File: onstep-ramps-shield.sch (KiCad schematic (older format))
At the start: 0 parts

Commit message: Schematic, initial board layout
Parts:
- added BME280, DS3231: Conn_01x08, Connector_PinSocket_2.54mm:PinSocket_1x08_P2.54mm_Vertical, symbol Connector_Generic:Conn_01x08
- added BZ1: Buzzer, Buzzer_Beeper:Buzzer_12x9.5RM7.6, symbol Device:Buzzer
- added DEC1, FOC1, FOC2, RA1: RJ12, Connector_RJ:RJ12_Amphenol_54601, symbol Connector:RJ12
- added J_AUX1: RAMPS_AUX1, Connector_PinSocket_2.54mm:PinSocket_2x04_P2.54mm_Vertical, symbol OnstepRampsShield:RAMPS_AUX1
- added J_AUX2: RAMPS_AUX2, Connector_PinSocket_2.54mm:PinSocket_2x05_P2.54mm_Vertical, symbol OnstepRampsShield:RAMPS_AUX2
- added J_AUX3: RAMPS_AUX3, Connector_PinSocket_2.54mm:PinSocket_2x04_P2.54mm_Vertical, symbol OnstepRampsShield:RAMPS_AUX3
- added J_AUX4: RAMPS_AUX-4, Connector_PinSocket_2.54mm:PinSocket_1x18_P2.54mm_Vertical, symbol OnstepRampsShield:RAMPS_AUX-4
- added J_DEC1, J_FOC1, J_FOC2, J_RA1: RAMPS_MOTOR, Connector_PinSocket_2.54mm:PinSocket_1x04_P2.54mm_Vertical, symbol OnstepRampsShield:RAMPS_MOTOR
- added J_I2C1: RAMPS_I2C, Connector_PinSocket_2.54mm:PinSocket_1x04_P2.54mm_Vertical, symbol OnstepRampsShield:RAMPS_I2C
- added J_PEC1, J_RET1: AudioJack3, Connector_Audio:Jack_3.5mm_CUI_SJ1-3533NG_Horizontal, symbol Connector:AudioJack3
- added J_SER1: RAMPS_ENDSTOPS, Connector_PinSocket_2.54mm:PinSocket_1x02_P2.54mm_Vertical, symbol OnstepRampsShield:RAMPS_ENDSTOPS
- added J_SERV1: RAMPS_SERVOS_SER1, Connector_PinSocket_2.54mm:PinSocket_1x03_P2.54mm_Vertical, symbol OnstepRampsShield:RAMPS_SERVOS_SER1
- added J_SERV2: RAMPS_SERVOS_SER2, Connector_PinSocket_2.54mm:PinSocket_1x03_P2.54mm_Vertical, symbol OnstepRampsShield:RAMPS_SERVOS_SER2
- added J_SERV3: RAMPS_SERVOS_SER3, Connector_PinSocket_2.54mm:PinSocket_1x03_P2.54mm_Vertical, symbol OnstepRampsShield:RAMPS_SERVOS_SER3
- added J_SERV4: RAMPS_SERVOS_SER4, Connector_PinSocket_2.54mm:PinSocket_1x03_P2.54mm_Vertical, symbol OnstepRampsShield:RAMPS_SERVOS_SER4
- added R1: 2k, Resistor_THT:R_Axial_DIN0204_L3.6mm_D1.6mm_P5.08mm_Horizontal, symbol Device:R
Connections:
- new net: BZ1.2 (+), J_SERV4.1 (GND)
- new net: BZ1.1 (-), J_SERV4.3 (D4)
- new net: J_RET1.S, R1.2
- new net CS_BME280: BME280.7 (Pin_7), J_AUX3.2 (D49)
- new net CS_DS3234: J_AUX3.6 (D53)
- new net E0_1A: FOC1.3, J_FOC1.3 (1A)
- new net E0_1B: FOC1.4, J_FOC1.4 (1B)
- new net E0_2A: FOC1.2, J_FOC1.2 (2A)
- new net E0_2B: FOC1.1, J_FOC1.1 (2B)
- new net E1_1A: FOC2.3, J_FOC2.3 (1A)
- new net E1_1B: FOC2.4, J_FOC2.4 (1B)
- new net E1_2A: FOC2.2, J_FOC2.2 (2A)
- new net E1_2B: FOC2.1, J_FOC2.1 (2B)
- new net GND: BME280.1 (Pin_1), DS3231.1 (Pin_1), J_AUX1.3 (GND), J_AUX1.4 (GND), J_AUX2.2 (GND), J_AUX3.7 (GND), J_AUX4.2 (GND), J_I2C1.2 (GND), J_PEC1.S, J_SERV1.1 (GND), J_SERV2.1 (GND), J_SERV3.1 (GND)
- new net PEC: J_AUX1.5 (A3), J_PEC1.R
- new net RETICULE_LED: J_SERV3.3 (D5), R1.1
- new net RX1: J_SER1.2 (D19)
- new net RX2: J_AUX4.17 (D17)
- new net SCK: BME280.4 (Pin_4), J_AUX3.5 (SCK)
- new net SCL: DS3231.4 (Pin_4), J_I2C1.4 (SCL)
- new net SDA: DS3231.3 (Pin_3), J_I2C1.3 (SDA)
- new net SDI: BME280.6 (Pin_6), J_AUX3.3 (MISO)
- new net SDO: BME280.5 (Pin_5), J_AUX3.4 (MOSI)
- new net STATUS_LED: J_SERV1.3 (D11)
- new net STATUS_LED2: J_SERV2.3 (D6)
- new net TX1: J_SER1.1 (D18)
- new net TX2: J_AUX4.18 (D16)
- new net VCC: BME280.3 (Pin_3), DS3231.2 (Pin_2), J_AUX1.1 (VCC), J_AUX1.2 (VCC), J_AUX2.1 (VCC), J_AUX3.1 (VCC), J_AUX4.1 (VCC), J_I2C1.1 (VCC), J_PEC1.T, J_RET1.T, J_SERV1.2 (VCC), J_SERV2.2 (VCC), J_SERV3.2 (VCC), J_SERV4.2 (VCC)
- new net X_1A: J_RA1.3 (1A), RA1.3
- new net X_1B: J_RA1.4 (1B), RA1.4
- new net X_2A: J_RA1.2 (2A), RA1.2
- new net X_2B: J_RA1.1 (2B), RA1.1
- new net X_AUX1: J_AUX4.13 (D29)
- new net X_M0: J_AUX4.16 (D23)
- new net X_M1: J_AUX4.15 (D25)
- new net X_M2: J_AUX4.14 (D27)
- new net Y_1A: DEC1.3, J_DEC1.3 (1A)
- new net Y_1B: DEC1.4, J_DEC1.4 (1B)
- new net Y_2A: DEC1.2, J_DEC1.2 (2A)
- new net Y_2B: DEC1.1, J_DEC1.1 (2B)
- new net Y_AUX1: J_AUX4.9 (D37)
- new net Y_M0: J_AUX4.12 (D31)
- new net Y_M1: J_AUX4.11 (D33)
- new net Y_M2: J_AUX4.10 (D35)
- no-connect marks 0 -> 33

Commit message: Routing
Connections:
- net GND: now also BZ1.2 (+); no longer BME280.1 (Pin_1), DS3231.1 (Pin_1), J_AUX1.3 (GND), J_AUX1.4 (GND), J_AUX2.2 (GND), J_AUX3.7 (GND), J_I2C1.2 (GND), J_SERV1.1 (GND), J_SERV2.1 (GND), J_SERV3.1 (GND)
- net VCC: no longer BME280.3 (Pin_3), DS3231.2 (Pin_2), J_AUX1.1 (VCC), J_AUX1.2 (VCC), J_AUX2.1 (VCC), J_AUX3.1 (VCC), J_I2C1.1 (VCC), J_SERV1.2 (VCC), J_SERV2.2 (VCC), J_SERV3.2 (VCC), J_SERV4.2 (VCC)
- net at J_SERV4.1 (GND): no longer BZ1.2 (+)
- net BUZZER: now reaches BZ1.1 (-), J_SERV4.3 (D4)
- new net I2C_GND: DS3231.1 (Pin_1), J_I2C1.2 (GND)
- new net I2C_VCC: DS3231.2 (Pin_2), J_I2C1.1 (VCC)
- new net SPI_GND: BME280.1 (Pin_1), J_AUX3.7 (GND)
- new net SPI_VCC: BME280.3 (Pin_3), J_AUX3.1 (VCC)
- no-connect marks 33 -> 47
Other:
- moved on the sheet: BZ1
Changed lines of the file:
@@
 	0    -1   -1   0
 $EndComp
-Text GLabel 2350 6700 0    50   Input ~ 0
-VCC
-Text GLabel 3750 6750 0    50   Input ~ 0
-VCC
 Text GLabel 5100 4650 0    50   Input ~ 0
 VCC
 Text GLabel 5550 2250 2    50   Input ~ 0
-VCC
-Text GLabel 2950 6700 2    50   Input ~ 0
-GND
-Text GLabel 3750 7050 0    50   Input ~ 0
-GND
+I2C_VCC
 Text GLabel 5100 4550 0    50   Input ~ 0
 GND
 Text GLabel 5550 2350 2    50   Input ~ 0
-GND
+I2C_GND
 Text GLabel 1000 1800 3    50   Input ~ 0
 E0_2B
@@
 L Device:Buzzer BZ1
 U 1 1 5F550329
-P 2600 5300
-F 0 "BZ1" V 2651 5113 50  0000 R CNN
-F 1 "Buzzer" V 2560 5113 50  0000 R CNN
-F 2 "Buzzer_Beeper:Buzzer_12x9.5RM7.6" V 2575 5400 50  0001 C CNN
-F 3 "~" V 2575 5400 50  0001 C CNN
-	1    2600 5300
-	0    -1   -1   0
-$EndComp
-Wire Wire Line
-	2500 5850 2500 5400
-Wire Wire Line
-	2700 5400 2700 5850
+P 7300 4100
+F 0 "BZ1" V 7351 3913 50  0000 R CNN
+F 1 "Buzzer" V 7260 3913 50  0000 R CNN
+F 2 "Buzzer_Beeper:Buzzer_12x9.5RM7.6" V 7275 4200 50  0001 C CNN
+F 3 "~" V 7275 4200 50  0001 C CNN
+	1    7300 4100
+	0    -1   -1   0
+$EndComp
 Text GLabel 4350 6950 2    50   Input ~ 0
 CS_DS3234
@@
 Text GLabel 7450 1250 2    50   Input ~ 0
 CS_BME280
-Text GLabel 7450 1850 2    50   Input ~ 0
-GND
-Text GLabel 7450 1650 2    50   Input ~ 0
-VCC
-Text GLabel 7450 3200 2    50   Input ~ 0
-VCC
 Text GLabel 7450 3300 2    50   Input ~ 0
-GND
+I2C_GND
 Text GLabel 4350 6750 2    50   Input ~ 0
 CS_BME280
@@
 	0    -1   -1   0
 $EndComp
-Text GLabel 1450 6800 2    50   Input ~ 0
-GND
-Text GLabel 1450 6700 2    50   Input ~ 0
-VCC
-Text GLabel 850  6800 0    50   Input ~ 0
-GND
-Text GLabel 850  6700 0    50   Input ~ 0
-VCC
-Text GLabel 2700 4500 1    50   Input ~ 0
-GND
-Text GLabel 2600 4500 1    50   Input ~ 0
-VCC
-Text GLabel 2600 5850 1    50   Input ~ 0
-VCC
-Text GLabel 1250 5850 1    50   Input ~ 0
-GND
-Text GLabel 1150 5850 1    50   Input ~ 0
-VCC
-Text GLabel 1200 4500 1    50   Input ~ 0
-GND
-Text GLabel 1100 4500 1    50   Input ~ 0
-VCC
 $Comp
 L Connector_Generic:Conn_01x08 BME280
@@
 NoConn ~ 7450 2700
 NoConn ~ 7450 2600
+Text GLabel 7450 3200 2    50   Input ~ 0
+I2C_VCC
+Text GLabel 3750 6750 0    50   Input ~ 0
+SPI_VCC
+Text GLabel 3750 7050 0    50   Input ~ 0
+SPI_GND
+Text GLabel 7450 1650 2    50   Input ~ 0
+SPI_VCC
+Text GLabel 7450 1850 2    50   Input ~ 0
+SPI_GND
+NoConn ~ 2600 4500
+NoConn ~ 2700 4500
+NoConn ~ 1100 4500
+NoConn ~ 1200 4500
+NoConn ~ 1150 5850
+NoConn ~ 1250 5850
+NoConn ~ 2600 5850
+NoConn ~ 2700 5850
+Text GLabel 2500 5850 1    50   Input ~ 0
+BUZZER
+Text GLabel 7200 4200 3    50   Input ~ 0
+BUZZER
+Text GLabel 7400 4200 3    50   Input ~ 0
+GND
+NoConn ~ 2350 6700
+NoConn ~ 2950 6700
+NoConn ~ 850  6700
+NoConn ~ 850  6800
+NoConn ~ 1450 6800
+NoConn ~ 1450 6700
 $EndSCHEMATC

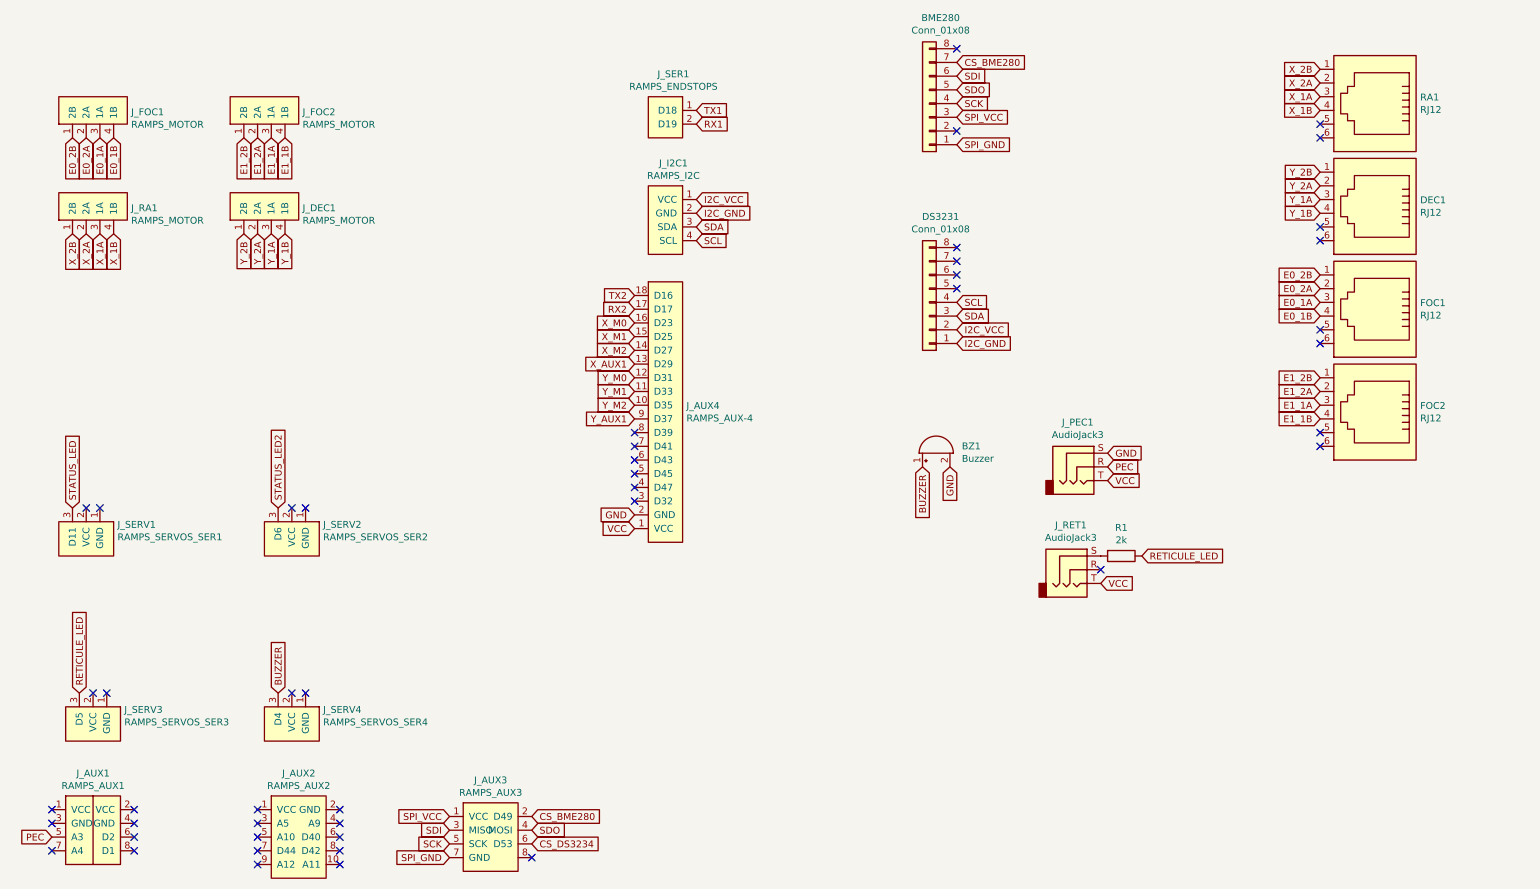
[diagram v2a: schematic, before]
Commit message: Include HC05
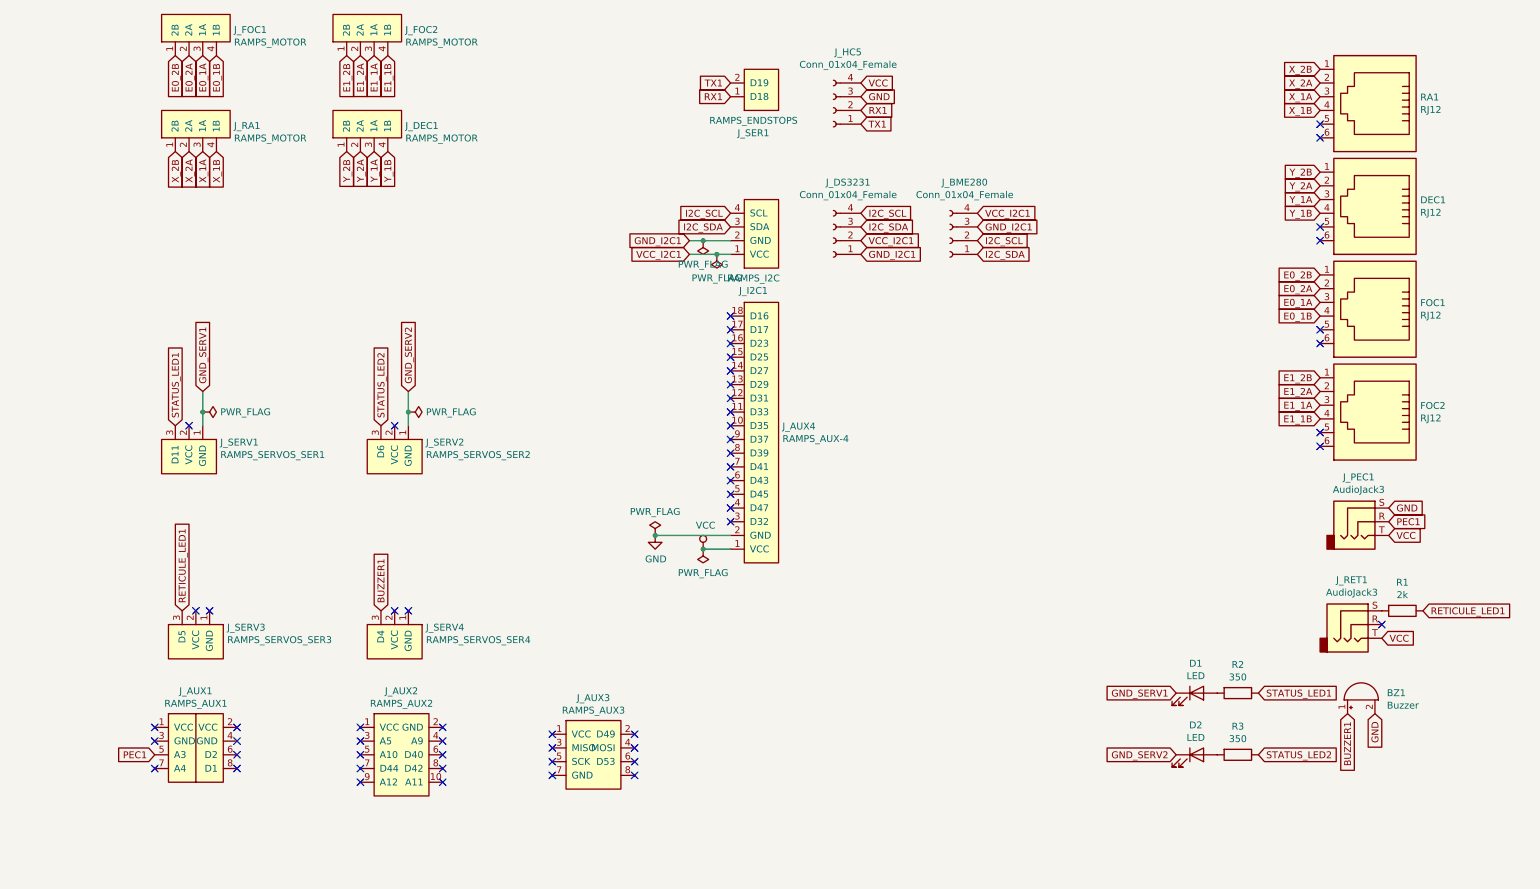
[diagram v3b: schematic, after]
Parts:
- removed BME280, DS3231: Conn_01x08, Connector_PinSocket_2.54mm:PinSocket_1x08_P2.54mm_Vertical, symbol Connector_Generic:Conn_01x08
- added D1, D2: LED, LED_SMD:LED_0603_1608Metric_Pad1.05x0.95mm_HandSolder, symbol Device:LED
- added J_BME280, J_DS3231, J_HC5: Conn_01x04_Female, Connector_PinSocket_2.54mm:PinSocket_1x04_P2.54mm_Vertical, symbol Connector:Conn_01x04_Female
- added R2, R3: 350, Resistor_SMD:R_0603_1608Metric_Pad1.05x0.95mm_HandSolder, symbol Device:R
- R1: footprint Resistor_THT:R_Axial_DIN0204_L3.6mm_D1.6mm_P5.08mm_Horizontal -> Resistor_SMD:R_0603_1608Metric_Pad1.05x0.95mm_HandSolder
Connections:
- net GND: now also J_HC5.3 (Pin_3)
- net RX1: now also J_SER1.1 (D18), J_HC5.2 (Pin_2); no longer J_SER1.2 (D19)
- net STATUS_LED2: now also R3.1
- net TX1: now also J_SER1.2 (D19), J_HC5.1 (Pin_1); no longer J_SER1.1 (D18)
- net VCC: now also J_HC5.4 (Pin_4)
- net GND_SERV1: now reaches J_SERV1.1 (GND)
- net GND_SERV1: now also D1.1 (K)
- net GND_SERV2: now reaches J_SERV2.1 (GND)
- net GND_SERV2: now also D2.1 (K)
- net BUZZER renamed BUZZER1
- net CS_BME280: no longer names the net of J_AUX3.2 (D49)
- net CS_DS3234: no longer names the net of J_AUX3.6 (D53)
- net I2C_GND renamed GND_I2C1
- net GND_I2C1: now also J_BME280.3 (Pin_3), J_DS3231.1 (Pin_1)
- net I2C_VCC renamed VCC_I2C1
- net VCC_I2C1: now also J_BME280.4 (Pin_4), J_DS3231.2 (Pin_2)
- net PEC renamed PEC1
- net RETICULE_LED renamed RETICULE_LED1
- net RX2: no longer names the net of J_AUX4.17 (D17)
- net SCK: no longer names the net of J_AUX3.5 (SCK)
- net SCL renamed I2C_SCL
- net I2C_SCL: now also J_BME280.2 (Pin_2), J_DS3231.4 (Pin_4)
- net SDA renamed I2C_SDA
- net I2C_SDA: now also J_BME280.1 (Pin_1), J_DS3231.3 (Pin_3)
- net SDI: no longer names the net of J_AUX3.3 (MISO)
- net SDO: no longer names the net of J_AUX3.4 (MOSI)
- net SPI_GND: no longer names the net of J_AUX3.7 (GND)
- net SPI_VCC: no longer names the net of J_AUX3.1 (VCC)
- net STATUS_LED renamed STATUS_LED1
- net STATUS_LED1: now also R2.1
- net TX2: no longer names the net of J_AUX4.18 (D16)
- net X_AUX1: no longer names the net of J_AUX4.13 (D29)
- net X_M0: no longer names the net of J_AUX4.16 (D23)
- net X_M1: no longer names the net of J_AUX4.15 (D25)
- net X_M2: no longer names the net of J_AUX4.14 (D27)
- net Y_AUX1: no longer names the net of J_AUX4.9 (D37)
- net Y_M0: no longer names the net of J_AUX4.12 (D31)
- net Y_M1: no longer names the net of J_AUX4.11 (D33)
- net Y_M2: no longer names the net of J_AUX4.10 (D35)
- new net: D1.2 (A), R2.2
- new net: D2.2 (A), R3.2
- no-connect marks 47 -> 56
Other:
- moved on the sheet: BZ1, J_AUX1, J_AUX2, J_AUX3, J_AUX4, J_DEC1, J_FOC1, J_FOC2, J_I2C1, J_PEC1, J_RA1, J_RET1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

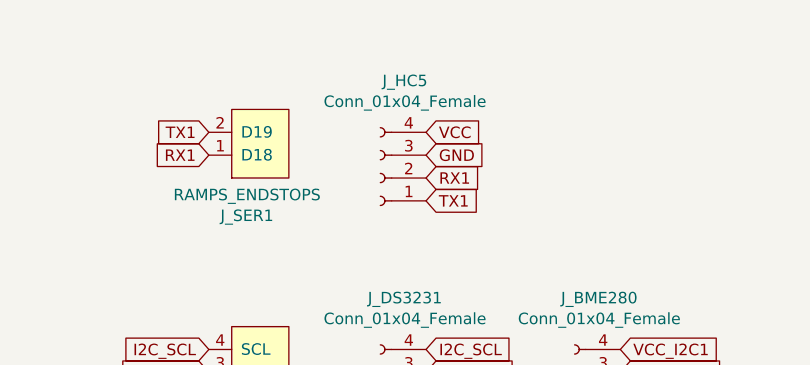
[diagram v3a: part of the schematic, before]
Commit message: Reorder components
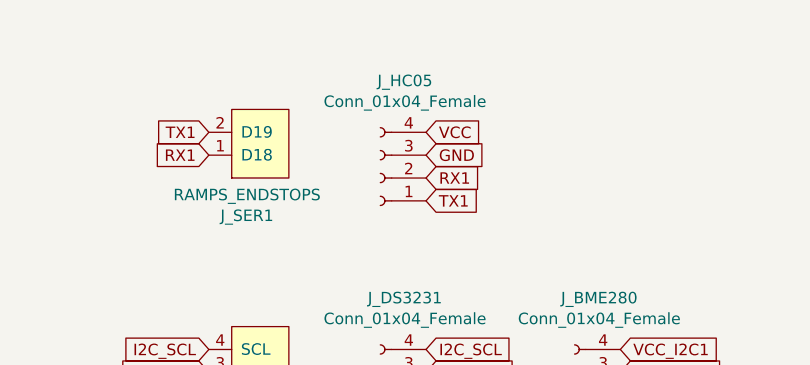
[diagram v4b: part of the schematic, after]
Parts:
- renumbered J_HC5 to J_HC05
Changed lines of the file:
@@
 $EndComp
 $Comp
-L Connector:Conn_01x04_Female J_HC5
+L Connector:Conn_01x04_Female J_HC05
 U 1 1 5F53C3AF
 P 6550 1600
-F 0 "J_HC5" H 6442 1175 50  0000 C CNN
+F 0 "J_HC05" H 6442 1175 50  0000 C CNN
 F 1 "Conn_01x04_Female" H 6442 1266 50  0000 C CNN
 F 2 "Connector_PinSocket_2.54mm:PinSocket_1x04_P2.54mm_Vertical" H 6550 1600 50  0001 C CNN

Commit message: Update connectors
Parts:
- J_PEC1, J_RET1: footprint Connector_Audio:Jack_3.5mm_CUI_SJ1-3533NG_Horizontal -> Connector_Audio:Jack_3.5mm_CUI_SJ1-3533NG_Horizontal_CircularHoles
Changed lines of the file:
@@
 F 0 "J_PEC1" H 10382 4925 50  0000 C CNN
 F 1 "AudioJack3" H 10382 4834 50  0000 C CNN
-F 2 "Connector_Audio:Jack_3.5mm_CUI_SJ1-3533NG_Horizontal" H 10400 4600 50  0001 C CNN
+F 2 "Connector_Audio:Jack_3.5mm_CUI_SJ1-3533NG_Horizontal_CircularHoles" H 10400 4600 50  0001 C CNN
 F 3 "~" H 10400 4600 50  0001 C CNN
 	1    10400 4600
@@
 F 0 "J_RET1" H 10332 5675 50  0000 C CNN
 F 1 "AudioJack3" H 10332 5584 50  0000 C CNN
-F 2 "Connector_Audio:Jack_3.5mm_CUI_SJ1-3533NG_Horizontal" H 10350 5350 50  0001 C CNN
+F 2 "Connector_Audio:Jack_3.5mm_CUI_SJ1-3533NG_Horizontal_CircularHoles" H 10350 5350 50  0001 C CNN
 F 3 "~" H 10350 5350 50  0001 C CNN
 	1    10350 5350
